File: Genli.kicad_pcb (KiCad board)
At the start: 2 copper layers, 110 x 80 mm, 20 parts, among them J1 Screw_Terminal_01x02, U1 ICM-20948, U2 VL53L0X, U3 VL53L0X

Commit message: touch up pcb layout
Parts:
- moved U11 59.2 mm to (157.2, 68.0)
- moved U13 59.2 mm to (161.8, 68.0)
- moved U5 59.2 mm to (148.0, 68.0)
- moved U6 59.2 mm to (152.6, 68.0)
- moved U9 55.9 mm to (188.0, 120.0), turned to -90 degrees
- moved U15 45.7 mm to (138.6, 119.5), turned to -90 degrees
- moved U3 23.4 mm to (186.0, 84.0), turned to 0 degrees
- moved J1 23.0 mm to (176.5, 58.4)
- moved U2 22.0 mm to (177.0, 84.0)
- moved U8 8.66 mm to (191.3, 75.6), turned to -90 degrees

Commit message: update pcb trace
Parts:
- moved J1 2.85 mm to (179.0, 57.0), turned to 180 degrees
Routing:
- net /TOF2_XSHUT: track 0.00 -> 105.2 mm
- net /I2C_SDA: track 0.00 -> 96.9 mm
- net /GND: track 0.00 -> 90.1 mm
- net /TOF1_XSHUT: track 0.00 -> 85.7 mm
- net /I2C_SCL: track 0.00 -> 78.8 mm
- net /ESC3_SIG: track 0.00 -> 72.7 mm
- net /VBAT: track 0.00 -> 71.5 mm
- net /ESC4_SIG: track 0.00 -> 63.1 mm
- net /ESC2_SIG: track 0.00 -> 60.5 mm
- net /ESC1_SIG: track 0.00 -> 57.0 mm
- net /IMU_INT: track 0.00 -> 38.2 mm
- net /IMU_MOSI: track 0.00 -> 29.5 mm
- net Net-(J1-Pin_1): track 0.00 -> 23.7 mm
- net /IMU_MISO: track 0.00 -> 19.9 mm
- net /IMU_SCLK: track 0.00 -> 19.8 mm
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
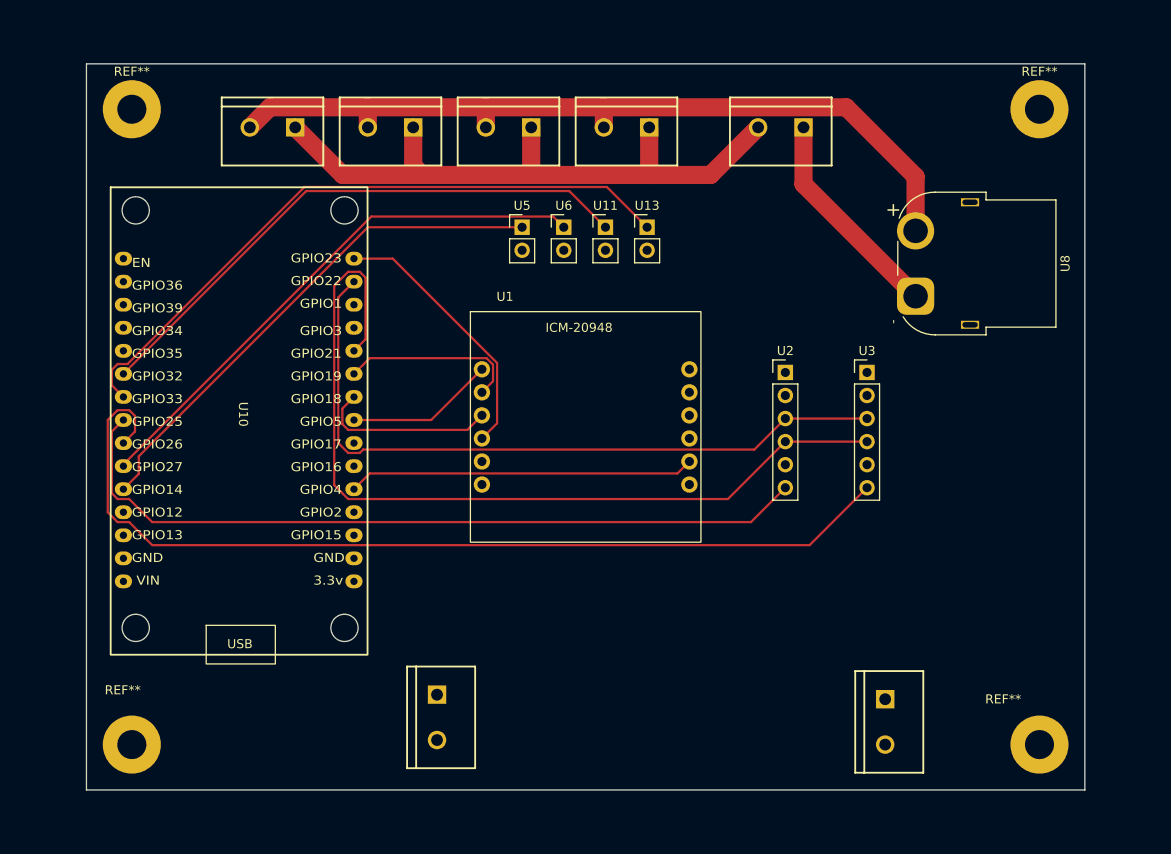
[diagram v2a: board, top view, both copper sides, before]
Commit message: update pcb layout with cleaner traces; switch esc +/- connectors to soldered pad instead of screw terminal
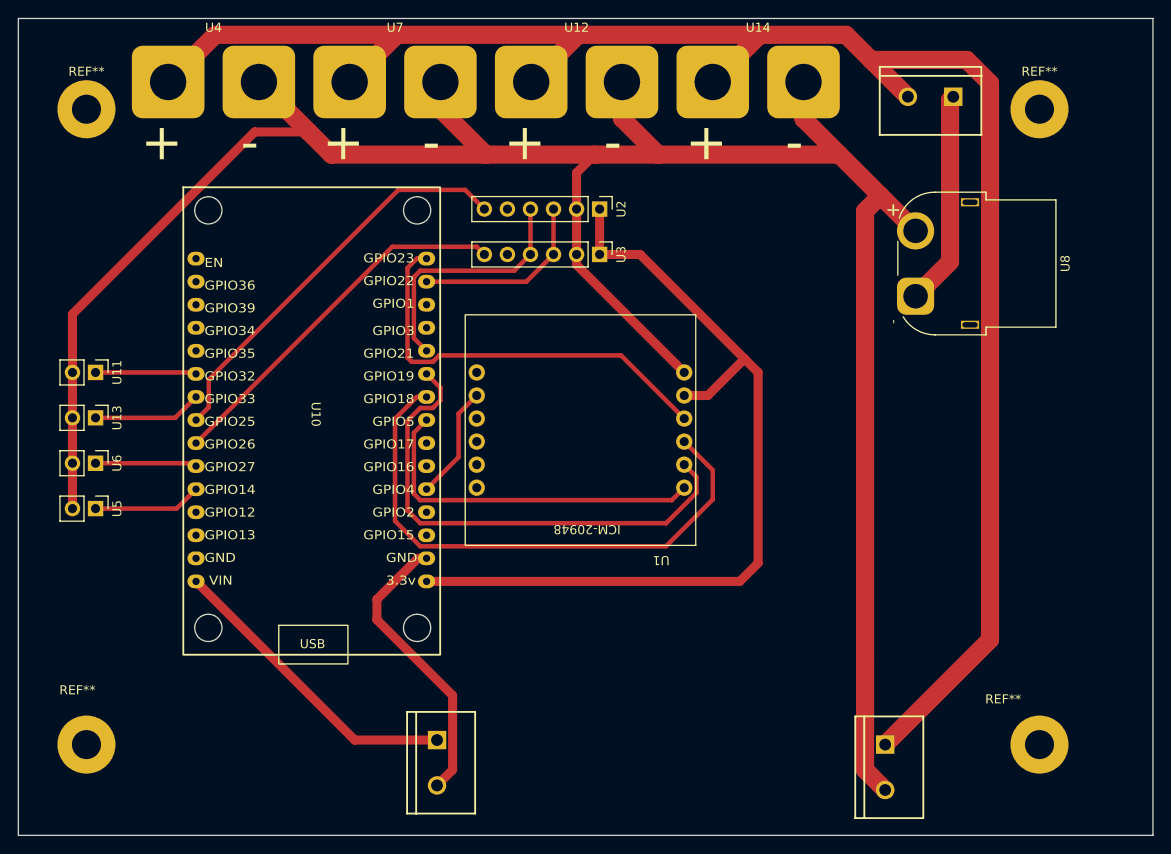
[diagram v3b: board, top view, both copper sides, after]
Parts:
- U12, U14, U4, U7: footprint PCM_SparkFun-Connector:ScrewTerminal_1x02_P5.0mm -> HopCopter:ESC_Power_SolderPads_1x02
- moved U13 64.3 mm to (101.0, 89.0), turned to -90 degrees
- moved U11 58.4 mm to (101.0, 84.0), turned to -90 degrees
- moved U6 57.8 mm to (101.0, 94.0), turned to -90 degrees
- moved U5 56.3 mm to (101.0, 99.0), turned to -90 degrees
- moved U3 32.2 mm to (156.5, 71.0), turned to -90 degrees
- moved U2 27.3 mm to (156.5, 66.0), turned to -90 degrees
- moved U1 25.8 mm to (165.9, 96.7), turned to 180 degrees
- moved J1 16.8 mm to (195.5, 53.6)
- moved U14 13.0 mm to (174.0, 52.0), turned to 0 degrees
- moved U4 10.3 mm to (114.0, 52.0), turned to 0 degrees
- moved U10 8.00 mm to (124.0, 90.0)
- moved U12 7.07 mm to (154.0, 52.0), turned to 0 degrees
- moved U7 5.39 mm to (134.0, 52.0), turned to 0 degrees
- moved REF** 5.00 mm to (100.0, 125.0)
- moved REF** 5.00 mm to (100.0, 55.0)
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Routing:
- net /GND: track 90.1 -> 261.1 mm
- net /VBAT: track 71.5 -> 200.1 mm
- net /ESP_3.3V: track 0.00 -> 94.5 mm
- net /I2C_SDA: track 96.9 -> 27.6 mm
- net /TOF2_XSHUT: track 105.2 -> 41.1 mm
- net /ESC3_SIG: track 72.7 -> 12.0 mm
- net /I2C_SCL: track 78.8 -> 20.2 mm
- net /ESC4_SIG: track 63.1 -> 11.1 mm
- net /ESC2_SIG: track 60.5 -> 11.2 mm
- net /ESC1_SIG: track 57.0 -> 12.0 mm
- net /IMU_SCLK: track 19.8 -> 61.7 mm
- net /TOF1_XSHUT: track 85.7 -> 44.9 mm
- net /IMU_MISO: track 19.9 -> 55.5 mm
- net Net-(U10-VIN): track 0.00 -> 33.8 mm
- net Net-(U15-GND): track 0.00 -> 32.0 mm
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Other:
- board size 110 x 80 mm -> 125 x 90 mm
